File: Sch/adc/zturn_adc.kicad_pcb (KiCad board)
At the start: 4 copper layers, 86 x 75.8 mm, 117 parts, among them CN1 SMA, CN2 SMA, CN3 AudioJack, J1 JP4, J2 Header5, J3 JP2, J4 JP2, J5 JP2, J6 JP2, P1 CONN_02X40, U1 LTC2292, U2 BGA2818, U3 TLV702, U4 BGA2818, U5 CDCLVC1102, U6 NAU8822LYG, U7 TLV702, X1 SIT5001

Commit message: Start redesign of ADC board
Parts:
- removed C48, C49: 1uF, adc_lib:C0603
- removed J5, J6: JP2, adc_lib:M20-9980245
- removed L11, L5, L6, L8, L9: L, adc_lib:FB0805
- removed RFTransformer1: MABAES0060, adc_lib:MABAES0060
- removed RN5: 22, adc_lib:EXB-38V220JV
- removed U7: TLV702, adc_lib:TLV702
- removed W1: TEST_1P, adc_lib:68000-401HLF
- added R31, R32: 12, adc_lib:R0402, F.Cu at (134.5, 140.9)
- added R33: 0, adc_lib:R0603, F.Cu at (134.5, 140.9)
- added R34: 680, adc_lib:R0603, F.Cu at (134.5, 140.9)
- added T1: ETC1-1-13, adc_lib:ETC1-1-13, F.Cu at (106.2, 98.4)
- added TP1, TP2, TP3, TP4: TEST, adc_lib:TL, F.Cu at (134.5, 140.9)
- C1, C2: value 1uF -> 1uF X7R
- C12: value 22nF -> 1uF X7R
- C18: value 0.1uF -> 1000pF; footprint adc_lib:C0402 -> adc_lib:C0603
- C19: value 1uF -> 4.7u 6V
- C20: value 0.1uF -> 1uF X7R
- C22, C24: value 18p -> 0.1u
- C23: value 150pF -> 0.1u
- C25: value 22nF -> 0.1u
- C37: value 0.1u -> 8p; footprint adc_lib:C0603 -> adc_lib:C0402
- C39: value 12p -> 0.1u
- J1: value JP4 -> JP2; footprint adc_lib:M20-9980445 -> adc_lib:M20-9980245
- J2: value Header5 -> JP2; footprint adc_lib:M20-9990546 -> adc_lib:M20-9980245
- L2: value 220nH -> L; footprint adc_lib:L0603 -> adc_lib:FB0805
- L3: value 27nH -> 8.2u; footprint adc_lib:L0603 -> adc_lib:L1008
- L4: value 220nH -> 3.3u; footprint adc_lib:L0603 -> adc_lib:L1008
- R13: value 22 -> 33
- R14: value 22 -> 0
- R15: value DNL -> 10k
- R16: value 50 -> 10k
- R17: value 25 -> 1M
- R18, R19: footprint adc_lib:R0603 -> adc_lib:R0402
- R20: value 25 -> 0
- R3, R9: value 10k -> 22
- U2: value BGA2818 -> LP5907_SOT-23; footprint adc_lib:BGA2818 -> adc_lib:LP5907
- U3: value TLV702 -> LP5907_SOT-23; footprint adc_lib:TLV702 -> adc_lib:LP5907
- U4: value BGA2818 -> NC7SVU04-SC70; footprint adc_lib:BGA2818 -> adc_lib:NC7SVU04-5SC70
- U5: value CDCLVC1102 -> NC7SVU04-SC70; footprint adc_lib:CDCLVC1102 -> adc_lib:NC7SVU04-5SC70
- X1: value SIT5001 -> TCXO; footprint adc_lib:SIT5001 -> adc_lib:TCXO
- moved R9 61.9 mm to (148.2, 56.3), turned to 0 degrees
- moved R4 59.3 mm to (142.3, 58.8), turned to 0 degrees
- moved L2 55.2 mm to (156.8, 94.9), turned to 0 degrees
- moved C20 45.7 mm to (109.0, 70.0), turned to 0 degrees
- moved L1 44.4 mm to (116.4, 115.2), turned to 135 degrees
- moved C39 36.5 mm to (105.8, 75.9)
- moved C38 33.1 mm to (97.4, 72.3)
- moved C12 31.7 mm to (115.4, 118.8), turned to 135 degrees
- moved C9 28.5 mm to (117.1, 121.5), turned to 135 degrees
- moved R3 27.6 mm to (139.2, 58.4)
- moved R16 27.0 mm to (101.3, 83.9), turned to 0 degrees
- moved L3 26.2 mm to (101.4, 72.1), turned to 90 degrees
- moved C22 24.8 mm to (122.5, 113.8), turned to 135 degrees
- moved U2 24.1 mm to (108.6, 73.3)
- moved L4 22.2 mm to (101.4, 76.5), turned to 90 degrees
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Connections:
- C1 pad 1: /RF_in/VCC33 -> /RF_in/VCC5
- C12 pad 1: Net-(C12-Pad1) -> /RF_in/VCC5
- C13 pad 1: /RF_in/VCC33 -> Net-(C13-Pad1)
- C14 pad 1: /RF_in/VCC33 -> Net-(C13-Pad1)
- C18 pad 2: GND -> Net-(C18-Pad2)
- C19 pad 1: Net-(C18-Pad1) -> Net-(C19-Pad1)
- C2 pad 1: Net-(C2-Pad1) -> VDD3
- C20 pad 1: Net-(C18-Pad1) -> Net-(C19-Pad1)
- C22 pad 1: Net-(C22-Pad1) -> Net-(C19-Pad1)
- C22 pad 2: Net-(C22-Pad2) -> GND
- C23 pad 1: Net-(C22-Pad1) -> Net-(C19-Pad1)
- C24 pad 1: Net-(C24-Pad1) -> GND
- C37 pad 2: GND -> Net-(C37-Pad2)
- C38 pad 1: Net-(C38-Pad1) -> +5V
- C39 pad 2: Net-(C39-Pad2) -> GND
- C9 pad 1: Net-(C9-Pad1) -> GND
- CN1 pad 1: Net-(CN1-Pad1) -> Net-(C26-Pad2)
- CN2 pad 1: Net-(C9-Pad2) -> Net-(C15-Pad2)
- J2 pad 1: /CN/JTAG_TCK -> +3V3
- J2 pad 2: /CN/JTAG_TMS -> +5V
- J2 pad 3: /CN/JTAG_TDI -> GND
- J2 pad 4: /CN/JTAG_TDO -> GND
- L1 pad 1: /RF_in/VCC33 -> Net-(C19-Pad1)
- L1 pad 2: +3V3 -> Net-(C9-Pad2)
- L10 pad 2: Net-(C49-Pad1) -> VDD3
- L2 pad 1: Net-(C22-Pad2) -> Net-(C13-Pad1)
- L2 pad 2: Net-(CN1-Pad1) -> +3V3
- L3 pad 1: Net-(C22-Pad1) -> Net-(C39-Pad1)
- L3 pad 2: GND -> +5V
- L4 pad 1: Net-(C24-Pad2) -> /RF_in/VCC5
- L4 pad 2: Net-(C22-Pad1) -> Net-(C39-Pad1)
- L7 pad 1: Net-(C48-Pad1) -> Net-(C28-Pad1)
- P1 pad 10: /CN/JTAG_TDI -> (no net)
- P1 pad 12: /CN/JTAG_TDO -> (no net)
- P1 pad 14: /CN/JTAG_NRST -> (no net)
- P1 pad 18: /CN/IO_B13_LN14 -> (no net)
- P1 pad 39: /CN/IO_B34_LN6 -> (no net)
- P1 pad 45: /CN/IO_B34_LP11(CLK?) -> (no net)
- P1 pad 46: Net-(P1-Pad46) -> (no net)
- P1 pad 48: Net-(P1-Pad48) -> (no net)
- P1 pad 49: Net-(P1-Pad49) -> (no net)
- P1 pad 5: /CN/VDD18_KEY_BACKUP -> (no net)
- P1 pad 50: Net-(P1-Pad50) -> (no net)
- P1 pad 51: Net-(P1-Pad51) -> (no net)
- P1 pad 52: Net-(P1-Pad52) -> (no net)
- P1 pad 53: Net-(P1-Pad53) -> (no net)
- P1 pad 55: Net-(P1-Pad55) -> (no net)
- P1 pad 56: Net-(P1-Pad56) -> (no net)
- P1 pad 57: Net-(P1-Pad57) -> (no net)
- P1 pad 58: Net-(P1-Pad58) -> (no net)
- P1 pad 59: Net-(P1-Pad59) -> (no net)
- P1 pad 6: /CN/JTAG_TCK -> (no net)
- P1 pad 60: Net-(P1-Pad60) -> (no net)
- P1 pad 61: Net-(P1-Pad61) -> (no net)
- P1 pad 62: Net-(P1-Pad62) -> (no net)
- P1 pad 63: Net-(P1-Pad63) -> (no net)
- P1 pad 64: Net-(P1-Pad64) -> (no net)
- P1 pad 65: Net-(P1-Pad65) -> (no net)
- P1 pad 66: Net-(P1-Pad66) -> (no net)
- P1 pad 69: Net-(P1-Pad69) -> (no net)
- P1 pad 70: Net-(P1-Pad70) -> (no net)
- P1 pad 71: Net-(P1-Pad71) -> (no net)
- P1 pad 72: Net-(P1-Pad72) -> (no net)
- P1 pad 73: Net-(P1-Pad73) -> (no net)
- P1 pad 74: Net-(P1-Pad74) -> (no net)
- P1 pad 75: Net-(P1-Pad75) -> (no net)
- P1 pad 76: Net-(P1-Pad76) -> (no net)
- P1 pad 77: Net-(P1-Pad77) -> (no net)
- P1 pad 78: Net-(P1-Pad78) -> (no net)
- P1 pad 79: Net-(P1-Pad79) -> (no net)
- P1 pad 8: /CN/JTAG_TMS -> (no net)
- P1 pad 80: Net-(P1-Pad80) -> /CN/BP
- P1 pad 9: /CN/IO_B13_LN11 -> (no net)
- R15 pad 1: Net-(C26-Pad2) -> /CN/BP
- R16 pad 1: /RF_in/VCMA -> /RF_in/VCC5
- R16 pad 2: Net-(C38-Pad1) -> Net-(R16-Pad2)
- R17 pad 1: Net-(R17-Pad1) -> Net-(R14-Pad2)
- R17 pad 2: Net-(C38-Pad1) -> Net-(C18-Pad2)
- R18 pad 1: Net-(C38-Pad1) -> Net-(R18-Pad1)
- R18 pad 2: Net-(R18-Pad2) -> Net-(C25-Pad2)
- R19 pad 1: Net-(R17-Pad1) -> Net-(C25-Pad2)
- R19 pad 2: Net-(C39-Pad1) -> Net-(R19-Pad2)
- R2 pad 1: /RF_in/VCC33 -> /RF_in/VCC5
- R20 pad 1: Net-(R18-Pad2) -> Net-(C25-Pad2)
- R20 pad 2: Net-(C39-Pad2) -> /RF_in/VCMA
- R21 pad 1: +3V3 -> Net-(C28-Pad1)
- R22 pad 1: +3V3 -> Net-(C28-Pad1)
- R25 pad 2: Net-(J1-Pad5) -> Net-(R25-Pad2)
- R26 pad 1: Net-(J1-Pad5) -> Net-(R25-Pad2)
- R3 pad 1: Net-(C48-Pad1) -> /CN/IO_B34_LP6
- R3 pad 2: Net-(R3-Pad2) -> FS
- R4 pad 1: Net-(R4-Pad1) -> /CN/IO_B34_LP8
- R4 pad 2: Net-(R4-Pad2) -> BCLK
- R5 pad 1: /RF_in/VCMB -> Net-(R33-Pad2)
- R6 pad 1: /RF_in/VCMB -> Net-(R33-Pad2)
- R9 pad 1: Net-(C18-Pad1) -> /CN/IO_B34_LN8
- R9 pad 2: Net-(R9-Pad2) -> DACIN
- RN1 pad 1: Net-(RN1-Pad1) -> (no net)
- RN1 pad 2: Net-(RN1-Pad2) -> (no net)
- RN1 pad 7: Net-(RN1-Pad7) -> (no net)
- RN1 pad 8: Net-(RN1-Pad8) -> (no net)
- RN3 pad 4: Net-(RN3-Pad4) -> (no net)
- RN3 pad 5: Net-(RN3-Pad5) -> (no net)
- U1 pad 1: Net-(C39-Pad1) -> Net-(C37-Pad1)
- U1 pad 2: Net-(C39-Pad2) -> Net-(C37-Pad2)
- U1 pad 24: Net-(U1-Pad24) -> (no net)
- U1 pad 25: Net-(U1-Pad25) -> (no net)
- U1 pad 26: Net-(U1-Pad26) -> (no net)
- U1 pad 27: Net-(U1-Pad27) -> (no net)
- U1 pad 28: Net-(U1-Pad28) -> (no net)
- U1 pad 29: Net-(U1-Pad29) -> (no net)
- U1 pad 30: Net-(U1-Pad30) -> (no net)
- U1 pad 32: /RF_in/VCC33 -> Net-(C13-Pad1)
- U1 pad 33: Net-(U1-Pad33) -> (no net)
- U1 pad 34: Net-(U1-Pad34) -> (no net)
- U1 pad 35: Net-(U1-Pad35) -> (no net)
- U1 pad 36: Net-(U1-Pad36) -> (no net)
- U1 pad 37: Net-(U1-Pad37) -> (no net)
- U1 pad 38: Net-(U1-Pad38) -> (no net)
- U1 pad 39: Net-(U1-Pad39) -> (no net)
- U1 pad 40: Net-(U1-Pad40) -> (no net)
- U1 pad 41: Net-(U1-Pad41) -> (no net)
- U1 pad 42: Net-(U1-Pad42) -> (no net)
- U1 pad 49: /RF_in/VCC33 -> Net-(C13-Pad1)
- U2 pad 1: Net-(C25-Pad2) -> /RF_in/VCC5
- U2 pad 3: Net-(C26-Pad2) -> Net-(R16-Pad2)
- U2 pad 5: GND -> Net-(C19-Pad1)
- U3 pad 1: /RF_in/VCC33 -> /RF_in/VCC5
- U3 pad 5: Net-(C2-Pad1) -> VDD3
- U4 pad 1: Net-(C12-Pad1) -> (no net)
- U4 pad 2: GND -> Net-(C18-Pad2)
- U4 pad 3: /RF_in/AMP_OUT -> GND
- U4 pad 4: GND -> Net-(R14-Pad2)
- U4 pad 5: GND -> Net-(C19-Pad1)
- U5 pad 1: Net-(R4-Pad1) -> (no net)
- U5 pad 2: Net-(R9-Pad2) -> Net-(R14-Pad2)
- U5 pad 3: Net-(R13-Pad2) -> GND
- U5 pad 4: GND -> Net-(R13-Pad2)
- U5 pad 5: Net-(U5-Pad5) -> Net-(C19-Pad1)
- U6 pad 1: Net-(U6-Pad1) -> (no net)
- U6 pad 19: Net-(U6-Pad19) -> (no net)
- U6 pad 2: Net-(U6-Pad2) -> (no net)
- U6 pad 20: Net-(U6-Pad20) -> (no net)
- U6 pad 21: Net-(U6-Pad21) -> (no net)
- U6 pad 22: Net-(U6-Pad22) -> (no net)
- U6 pad 23: Net-(U6-Pad23) -> (no net)
- U6 pad 25: Net-(U6-Pad25) -> (no net)
- U6 pad 3: Net-(U6-Pad3) -> (no net)
- U6 pad 32: Net-(U6-Pad32) -> (no net)
- U6 pad 4: Net-(U6-Pad4) -> (no net)
- U6 pad 5: Net-(U6-Pad5) -> (no net)
- U6 pad 6: Net-(U6-Pad6) -> (no net)
- X1 pad 1: Net-(X1-Pad1) -> GND
- X1 pad 3: Net-(R4-Pad2) -> Net-(C18-Pad1)
- X1 pad 4: Net-(C18-Pad1) -> Net-(C9-Pad2)
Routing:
- net (no net): track 0.00 -> 225.1 mm, vias 0 -> 43
- net GND: track 624.4 -> 418.3 mm, vias 168 -> 116
- net /CN/JTAG_NRST: track 37.3 -> 0.00 mm, vias 2 -> 0
- net /CN/JTAG_TDO: track 34.1 -> 0.00 mm, vias 2 -> 0
- net /CN/JTAG_TDI: track 31.9 -> 0.00 mm, vias 2 -> 0
- net Net-(C13-Pad1): track 0.00 -> 29.5 mm, vias 0 -> 4
- net /CN/JTAG_TMS: track 28.1 -> 0.00 mm
- net /CN/JTAG_TCK: track 25.3 -> 0.00 mm
- net Net-(C18-Pad1): track 24.9 -> 6.81 mm, vias 2 -> 0
- net /CN/IO_B34_LN8: track 2.83 -> 20.2 mm, vias 0 -> 4
- net /RF_in/VCC33: track 17.1 -> 0.00 mm, vias 3 -> 0
- net Net-(C19-Pad1): track 0.00 -> 14.7 mm, vias 0 -> 1
- net Net-(C38-Pad1): track 13.6 -> 0.00 mm
- net +3V3: track 33.4 -> 21.1 mm, vias 14 -> 6
- net /CN/VDDIO_13_PL: track 34.1 -> 22.8 mm, vias 2 -> 1
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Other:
- board text removed: "TCK TMS TDI TDO TRST"
- board text removed: "VDDDIO_13_PL"

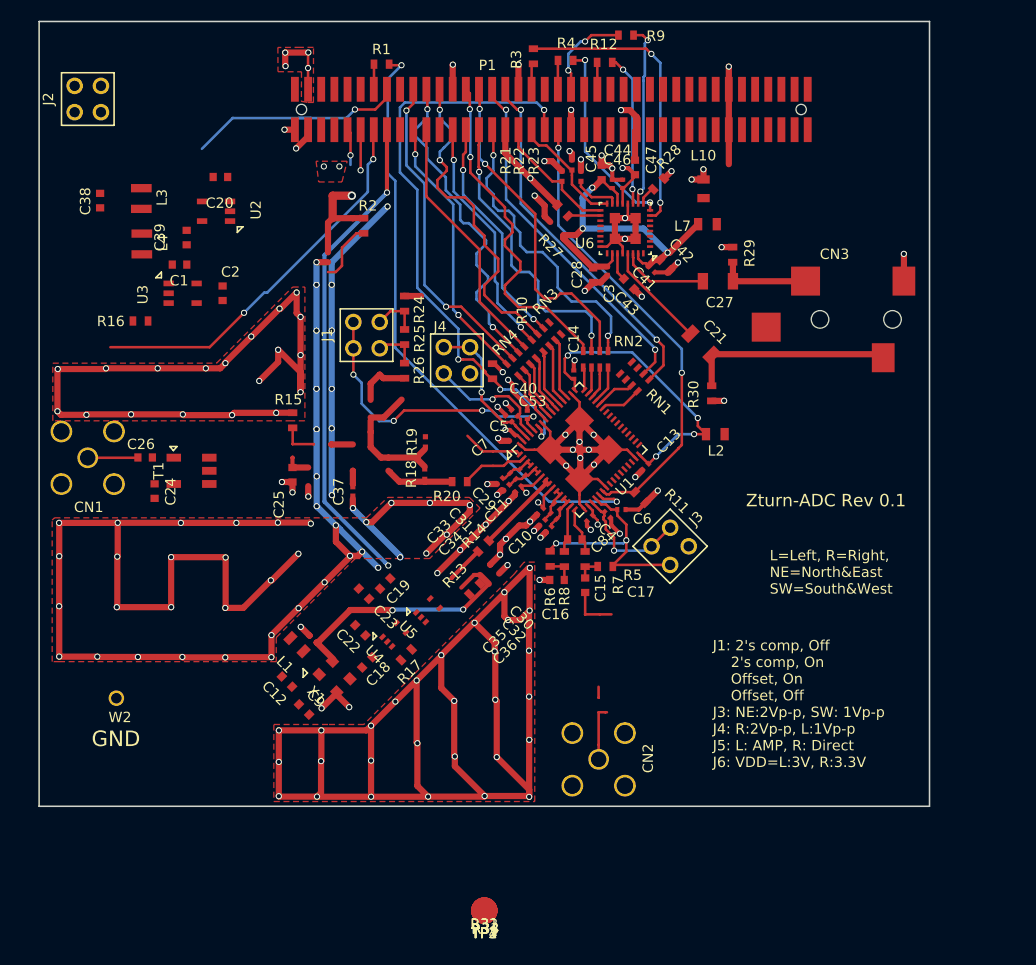
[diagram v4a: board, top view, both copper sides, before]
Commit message: ADC PCB layout in progress
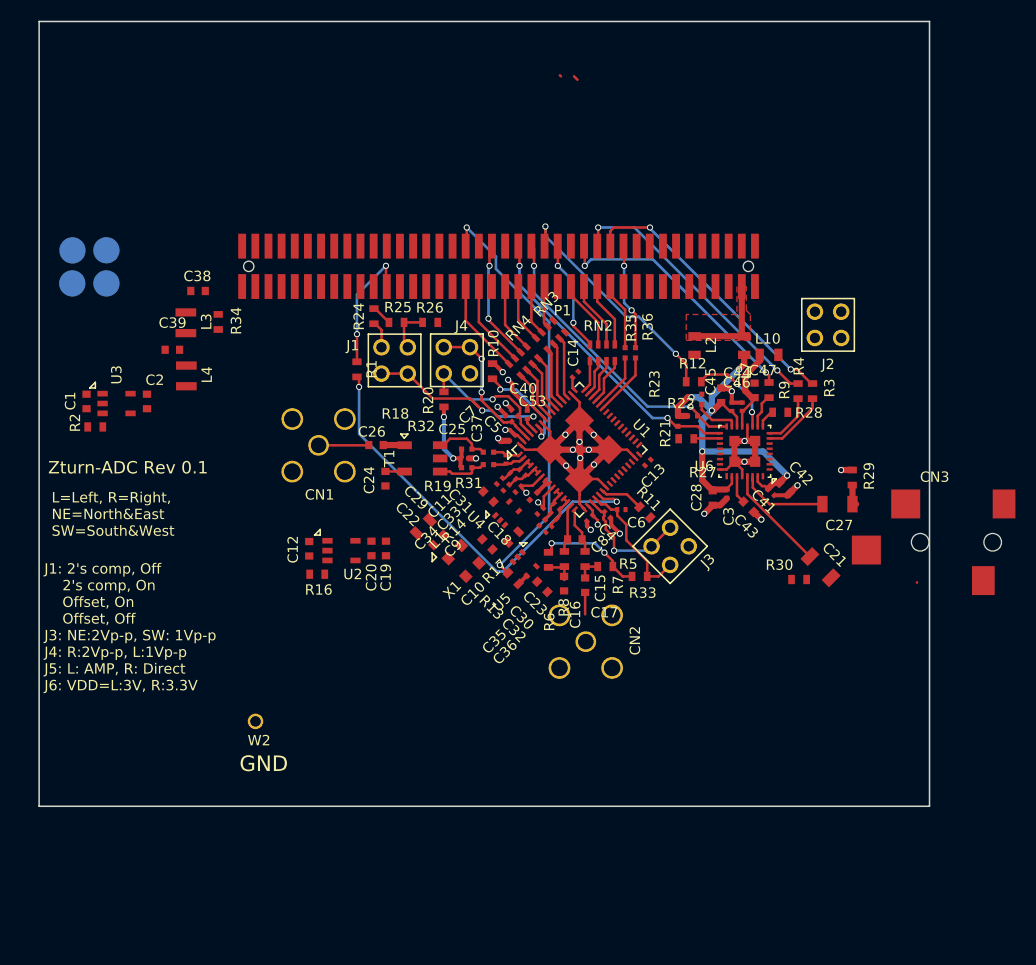
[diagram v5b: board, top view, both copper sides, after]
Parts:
- removed R15: 10k, adc_lib:R0603
- removed RN1: 22, adc_lib:EXB-38V220JV
- added R35: 22, adc_lib:R0402, F.Cu at (148.1, 87.0)
- added R36: 22, adc_lib:R0402, F.Cu at (149.1, 87.0)
- C25: footprint adc_lib:C0603 -> adc_lib:C0402
- R14: footprint adc_lib:R0603 -> adc_lib:R0402
- TP1, TP2, TP3, TP4: moved to B.Cu
- moved TP2 75.2 mm to (94.7, 77.1)
- moved J2 74.8 mm to (167.7, 84.3), turned to 0 degrees
- moved TP1 73.5 mm to (98.0, 77.1)
- moved TP4 72.5 mm to (94.7, 80.3)
- moved TP3 70.7 mm to (98.0, 80.3)
- moved R34 62.4 mm to (108.8, 84.0), turned to 90 degrees
- moved R32 44.3 mm to (134.9, 96.6), turned to 180 degrees
- moved R31 43.1 mm to (134.9, 97.8), turned to 180 degrees
- moved R3 42.1 mm to (166.2, 90.7), turned to 270 degrees
- moved R4 39.0 mm to (164.8, 90.7), turned to 270 degrees
- moved C20 38.7 mm to (123.6, 105.9), turned to 270 degrees
- moved R9 37.0 mm to (162.0, 90.6), turned to 270 degrees
- moved R33 35.6 mm to (149.5, 108.6), turned to 180 degrees
- moved U2 34.9 mm to (120.7, 106.1), turned to 270 degrees
- moved R2 32.4 mm to (96.9, 94.2), turned to 0 degrees
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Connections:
- net /CN/IO_B13_LP12(MRCC) renamed /CN/PS_MIO0
- P1 pad 13: /CN/IO_B13_LN12 -> (no net)
- P1 pad 15: /CN/VDDIO_13_PL -> (no net)
- P1 pad 16: ADC_CLK -> (no net)
- P1 pad 17: /CN/IO_B13_LP13(MRCC) -> (no net)
- P1 pad 19: /CN/IO_B13_LN13 -> (no net)
- P1 pad 20: /CN/IO_B13_LP21 -> GND
- P1 pad 21: /CN/IO_B13_LP15 -> GND
- P1 pad 22: /CN/IO_B13_LN21 -> /CN/IO_B35_LP2
- P1 pad 23: /CN/IO_B13_LN15 -> /CN/IO_B35_LP1
- P1 pad 24: GND -> /CN/IO_B35_LN2
- P1 pad 25: GND -> /CN/IO_B35_LN1
- P1 pad 26: /CN/IO_B34_LP1 -> /CN/IO_B35_LP4
- P1 pad 27: /CN/IO_B34_LP2 -> /CN/IO_B35_LP3
- P1 pad 28: /CN/IO_B34_LN1 -> /CN/IO_B35_LN4
- P1 pad 29: /CN/IO_B34_LN2 -> /CN/IO_B35_LN3
- P1 pad 30: /CN/IO_B34_LP3 -> GND
- P1 pad 31: /CN/IO_B34_LP4 -> GND
- P1 pad 32: /CN/IO_B34_LN3 -> /CN/IO_B35_LP6
- P1 pad 33: /CN/IO_B34_LN4 -> /CN/IO_B35_LP5
- P1 pad 34: GND -> /CN/IO_B35_LN6
- P1 pad 35: GND -> /CN/IO_B35_LN5
- P1 pad 36: SDA -> SCL
- P1 pad 37: /CN/IO_B34_LP6 -> /CN/IO_B35_LP7
- P1 pad 38: SCL -> SDA
- P1 pad 39: (no net) -> /CN/IO_B35_LN7
- P1 pad 40: /CN/SHDNA -> GND
- P1 pad 41: /CN/IO_B34_LP8 -> GND
- P1 pad 42: /CN/SHDNB -> /CN/IO_B35_LP10
- P1 pad 43: /CN/IO_B34_LN8 -> /CN/IO_B35_LP9
- P1 pad 44: GND -> (no net)
- P1 pad 45: (no net) -> /CN/IO_B35_LN9
- P1 pad 46: (no net) -> ADC_CLK
- P1 pad 47: /CN/IO_B34_LN11 -> (no net)
- P1 pad 50: (no net) -> GND
- P1 pad 54: GND -> (no net)
- P1 pad 57: (no net) -> /CN/IO_B35_LP15
- P1 pad 60: (no net) -> GND
- P1 pad 61: (no net) -> GND
- P1 pad 67: GND -> (no net)
- P1 pad 68: GND -> (no net)
- P1 pad 7: /CN/IO_B13_LP11(SRCC) -> (no net)
- P1 pad 70: (no net) -> GND
- P1 pad 71: (no net) -> GND
- P1 pad 76: (no net) -> /CN/IO_B35_LP24
- P1 pad 78: (no net) -> /CN/IO_B35_LN24
- P1 pad 79: (no net) -> /CN/IO_B35_LN23
- P1 pad 80: /CN/BP -> GND
- R1 pad 1: /CN/IO_B13_LN12 -> /CN/IO_B35_LP15
- R12 pad 2: /CN/IO_B34_LN11 -> /CN/IO_B35_LN6
- R3 pad 1: /CN/IO_B34_LP6 -> /CN/IO_B35_LN2
- R4 pad 1: /CN/IO_B34_LP8 -> /CN/IO_B35_LP4
- R9 pad 1: /CN/IO_B34_LN8 -> /CN/IO_B35_LN4
- RN2 pad 5: /CN/IO_B34_LN3 -> /CN/IO_B35_LN1
- RN2 pad 6: /CN/IO_B34_LN2 -> /CN/IO_B35_LP3
- RN2 pad 7: /CN/IO_B34_LP3 -> /CN/IO_B35_LN3
- RN2 pad 8: /CN/IO_B34_LP2 -> /CN/IO_B35_LP6
- RN3 pad 6: /CN/IO_B34_LN1 -> /CN/IO_B35_LP5
- RN3 pad 7: /CN/IO_B13_LN15 -> /CN/IO_B35_LN5
- RN3 pad 8: /CN/IO_B34_LP1 -> /CN/IO_B35_LP7
- RN4 pad 5: /CN/IO_B13_LN21 -> /CN/IO_B35_LN7
- RN4 pad 6: /CN/IO_B13_LP15 -> /CN/IO_B35_LP10
- RN4 pad 7: /CN/IO_B13_LN13 -> /CN/IO_B35_LP9
- RN4 pad 8: /CN/IO_B13_LP21 -> /CN/IO_B35_LN9
- TP2 pad 1: /CN/IO_B13_LP13(MRCC) -> /CN/IO_B35_LP24
- TP3 pad 1: /CN/IO_B13_LP11(SRCC) -> /CN/IO_B35_LN23
- TP4 pad 1: /CN/VDDIO_13_PL -> /CN/IO_B35_LN24
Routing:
- net GND: track 418.3 -> 81.7 mm, vias 116 -> 23
- net (no net): track 225.1 -> 14.4 mm, vias 43 -> 0
- net /CN/SHDNA: track 57.4 -> 9.99 mm, vias 4 -> 2
- net /CN/SHDNB: track 45.2 -> 4.24 mm, vias 2 -> 0
- net /CN/IO_B34_LN4: track 35.1 -> 0.00 mm, vias 2 -> 0
- net /CN/IO_B34_LP4: track 34.6 -> 0.00 mm, vias 2 -> 0
- net /CN/IO_B34_LP2: track 33.4 -> 0.00 mm, vias 2 -> 0
- net /CN/IO_B13_LN15: track 32.7 -> 0.00 mm, vias 2 -> 0
- net /CN/IO_B34_LN2: track 32.3 -> 0.00 mm, vias 2 -> 0
- net /CN/IO_B13_LP15: track 32.1 -> 0.00 mm, vias 2 -> 0
- net /CN/IO_B13_LN13: track 31.3 -> 0.00 mm, vias 2 -> 0
- net /CN/IO_B34_LN3: track 29.7 -> 0.00 mm, vias 2 -> 0
- net /CN/IO_B34_LP3: track 28.8 -> 0.00 mm, vias 2 -> 0
- net Net-(C13-Pad1): track 29.5 -> 1.54 mm, vias 4 -> 0
- net /CN/IO_B35_LN2: track 0.00 -> 27.4 mm, vias 0 -> 2
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- removed copper zone on F.Cu, net GND

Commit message: ADC Layout done except GND
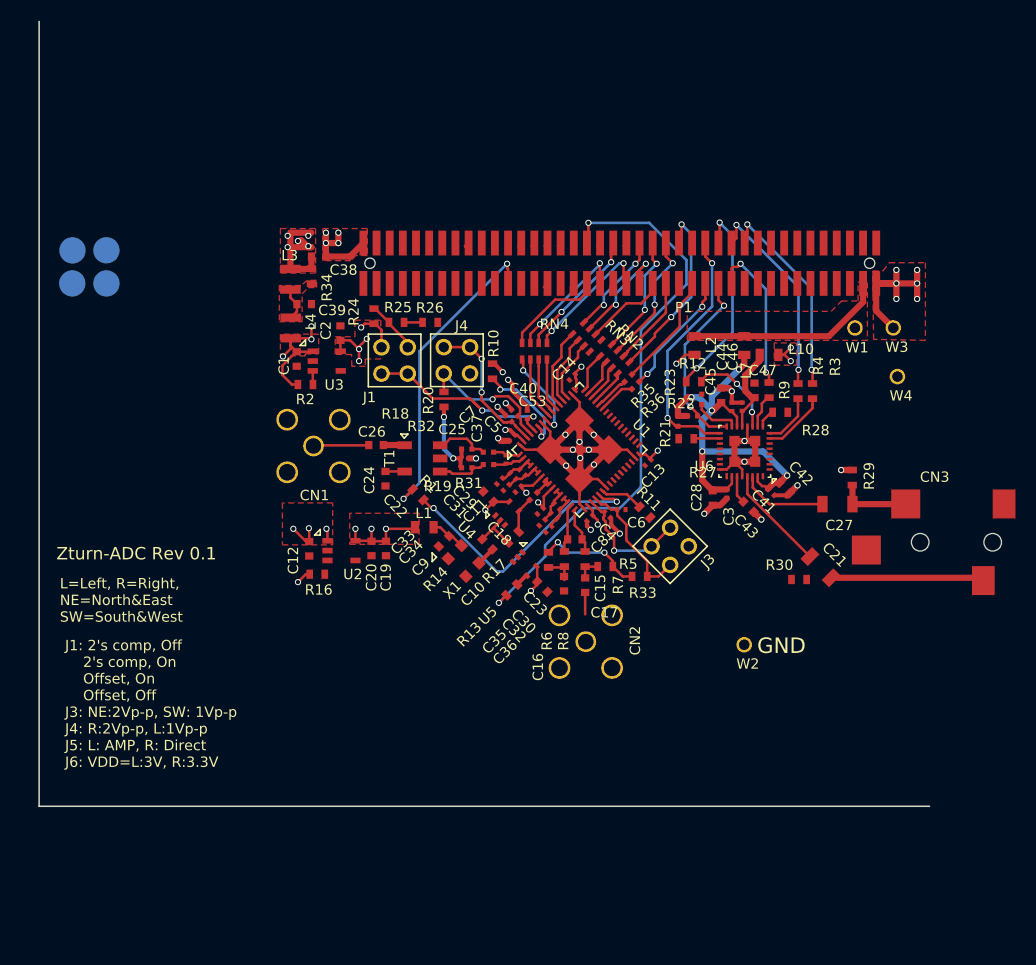
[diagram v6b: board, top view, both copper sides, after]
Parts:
- removed J2: JP2, adc_lib:M20-9980245
- added W1: TEST_1P, adc_lib:68000-401HLF, F.Cu at (170.3, 84.6)
- added W3: TEST_1P, adc_lib:68000-401HLF, F.Cu at (174.0, 84.6)
- added W4: TEST_1P, adc_lib:68000-401HLF, F.Cu at (174.4, 89.3)
- moved W2 47.8 mm to (159.6, 115.2)
- moved C1 20.7 mm to (116.4, 87.6)
- moved R2 20.7 mm to (117.2, 90.1)
- moved U3 20.7 mm to (119.3, 87.8)
- moved C2 19.8 mm to (120.6, 85.1), turned to 90 degrees
- moved C39 13.5 mm to (117.1, 82.3), turned to 0 degrees
- moved R1 13.5 mm to (128.1, 100.7), turned to 315 degrees
- moved C38 12.1 mm to (118.5, 77.7)
- moved P1 11.7 mm to (147.6, 78.3)
- moved L4 11.1 mm to (115.8, 84.6)
- moved L3 10.9 mm to (115.8, 79.9)
- moved R34 10.0 mm to (117.8, 79.6)
- moved RN3 3.51 mm to (144.4, 85.5), turned to 315 degrees
- moved R36 3.15 mm to (149.1, 90.2), turned to 225 degrees
- moved R35 2.47 mm to (148.4, 89.5), turned to 225 degrees
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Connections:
- P1 pad 25: /CN/IO_B35_LN1 -> SCL
- P1 pad 28: /CN/IO_B35_LN4 -> SDA
- P1 pad 36: SCL -> /CN/IO_B35_LP8
- P1 pad 38: SDA -> /CN/IO_B35_LN8
- R12 pad 2: /CN/IO_B35_LN6 -> /CN/IO_B35_LP4
- R3 pad 1: /CN/IO_B35_LN2 -> /CN/IO_B35_LP2
- R35 pad 1: /CN/IO_B35_LP1 -> /CN/IO_B35_LN3
- R36 pad 1: /CN/IO_B35_LP2 -> /CN/IO_B35_LP3
- R4 pad 1: /CN/IO_B35_LP4 -> /CN/IO_B35_LN2
- R9 pad 1: /CN/IO_B35_LN4 -> /CN/IO_B35_LP1
- RN2 pad 5: /CN/IO_B35_LN1 -> /CN/IO_B35_LP6
- RN2 pad 6: /CN/IO_B35_LP3 -> /CN/IO_B35_LP5
- RN2 pad 7: /CN/IO_B35_LN3 -> /CN/IO_B35_LN6
- RN2 pad 8: /CN/IO_B35_LP6 -> /CN/IO_B35_LP8
- RN3 pad 6: /CN/IO_B35_LP5 -> /CN/IO_B35_LN5
- RN3 pad 7: /CN/IO_B35_LN5 -> /CN/IO_B35_LP7
- RN3 pad 8: /CN/IO_B35_LP7 -> /CN/IO_B35_LN8
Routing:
- net +5V: track 0.00 -> 28.5 mm, vias 0 -> 8
- net /CN/IO_B35_LN4: track 25.4 -> 0.00 mm, vias 2 -> 0
- net /RF_in/VCC5: track 0.00 -> 19.2 mm, vias 0 -> 7
- net /CN/IO_B35_LP15: track 12.5 -> 30.0 mm
- net ADC_CLK: track 41.0 -> 57.0 mm
- net Net-(C21-Pad2): track 0.01 -> 14.8 mm
- net Net-(C19-Pad1): track 0.00 -> 14.7 mm, vias 0 -> 5
- net /CN/MUX: track 40.8 -> 26.3 mm
- net (no net): track 14.4 -> 1.96 mm, vias 0 -> 3
- net /CN/IO_B35_LP8: track 0.00 -> 11.7 mm, vias 0 -> 2
- net +3V3: track 8.50 -> 19.4 mm
- net /CN/IO_B35_LN6: track 23.3 -> 12.8 mm
- net SCL: track 28.7 -> 18.4 mm
- net /CN/IO_B35_LN8: track 0.00 -> 10.0 mm, vias 0 -> 2
- net VDD3: track 13.3 -> 23.3 mm, vias 4 -> 10
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- added copper zone on F.Cu, net +5V
- added copper zone on In2.Cu, net +5V
- added copper zone on F.Cu, net /RF_in/VCC5
- added copper zone on In2.Cu, net /RF_in/VCC5
- added copper zone on F.Cu, net GND
- added copper zone on In2.Cu, net Net-(C13-Pad1)
- added copper zone on F.Cu, net Net-(C19-Pad1)
- added copper zone on In2.Cu, net Net-(C19-Pad1)
- added copper zone on F.Cu, net Net-(C39-Pad1)
- added copper zone on F.Cu, net VDD3
- removed copper zone on In2.Cu, net +3V3
- removed copper zone on In2.Cu, net /AudioDAC/VDDC
- removed copper zone on In2.Cu, net /RF_in/VCC33
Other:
- outline, holes or cut-outs redrawn

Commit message: Improve layout
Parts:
- moved RN3 0.76 mm to (143.7, 85.6), turned to 0 degrees
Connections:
- P1 pad 35: /CN/IO_B35_LN5 -> (no net)
- P1 pad 37: /CN/IO_B35_LP7 -> (no net)
- P1 pad 38: /CN/IO_B35_LN8 -> (no net)
- P1 pad 39: /CN/IO_B35_LN7 -> (no net)
- P1 pad 42: /CN/IO_B35_LP10 -> (no net)
- P1 pad 48: (no net) -> /CN/IO_B35_LN12
- P1 pad 49: (no net) -> /CN/IO_B35_LN11
- P1 pad 52: (no net) -> /CN/IO_B35_LP14
- P1 pad 53: (no net) -> /CN/IO_B35_LP13(MRCC)
- P1 pad 55: (no net) -> /CN/IO_B35_LN13
- RN3 pad 6: /CN/IO_B35_LN5 -> /CN/IO_B35_LP9
- RN3 pad 7: /CN/IO_B35_LP7 -> /CN/IO_B35_LN9
- RN3 pad 8: /CN/IO_B35_LN8 -> /CN/IO_B35_LN12
- RN4 pad 5: /CN/IO_B35_LN7 -> /CN/IO_B35_LN11
- RN4 pad 6: /CN/IO_B35_LP10 -> /CN/IO_B35_LP14
- RN4 pad 7: /CN/IO_B35_LP9 -> /CN/IO_B35_LP13(MRCC)
- RN4 pad 8: /CN/IO_B35_LN9 -> /CN/IO_B35_LN13
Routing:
- net /CN/IO_B35_LN7: track 13.1 -> 0.00 mm, vias 2 -> 0
- net /CN/IO_B35_LP10: track 12.6 -> 0.00 mm, vias 2 -> 0
- net /CN/IO_B35_LP7: track 11.0 -> 0.00 mm, vias 2 -> 0
- net /CN/IO_B35_LP14: track 0.00 -> 10.1 mm, vias 0 -> 2
- net /CN/IO_B35_LN8: track 10.0 -> 0.00 mm, vias 2 -> 0
- net /CN/IO_B35_LN12: track 0.00 -> 8.69 mm, vias 0 -> 2
- net /CN/IO_B35_LN5: track 8.18 -> 0.00 mm
- net /CN/IO_B35_LP9: track 12.4 -> 5.22 mm, vias 2 -> 0
- net /CN/IO_B35_LN11: track 0.00 -> 6.30 mm
- net /CN/IO_B35_LP13(MRCC): track 0.00 -> 5.91 mm
- net /CN/IO_B35_LN13: track 0.00 -> 5.79 mm
- net /CN/IO_B35_LN9: track 9.70 -> 5.80 mm
- net Net-(RN3-Pad1): track 7.89 -> 6.47 mm
- net Net-(RN3-Pad2): track 6.98 -> 6.22 mm
